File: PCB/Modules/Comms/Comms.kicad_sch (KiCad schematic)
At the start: 51 parts, among them J1 In, J10 1PPS In, J11 32MHz Out, J12 Shield, J13 Shield, J14 BATT +, J15 BATT -, J2 Test, J3 Bus, J4 Bus, J5 SWD, J6 Shield, J7 Shield, J8 Shield, J9 Shield, Q1 Q_PMOS_GSD, U1 STM32WB09KEVx, U2 THVD1420D, U3 MLPF-NRG-01D3, Y1 32MHz, Y2 32.768k

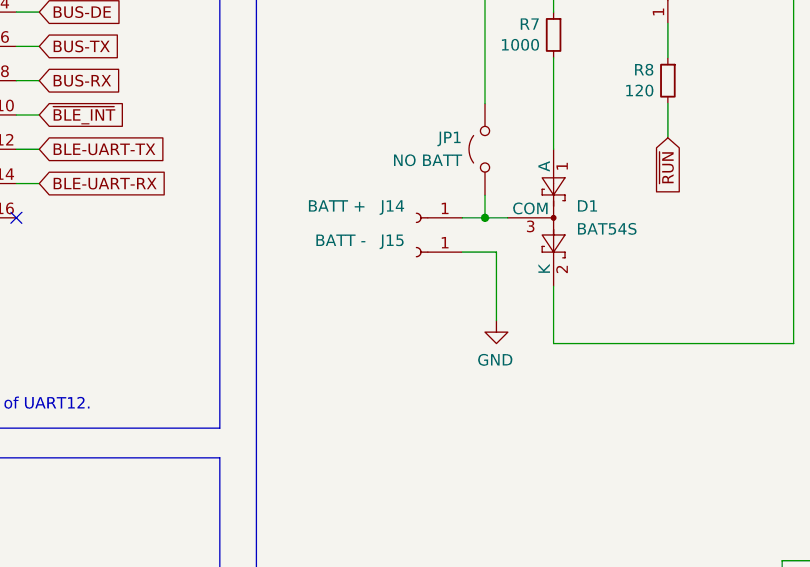
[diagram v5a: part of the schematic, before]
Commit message: feat: Replace bare pads for battery with a cell, incase we want to use a cell holder.
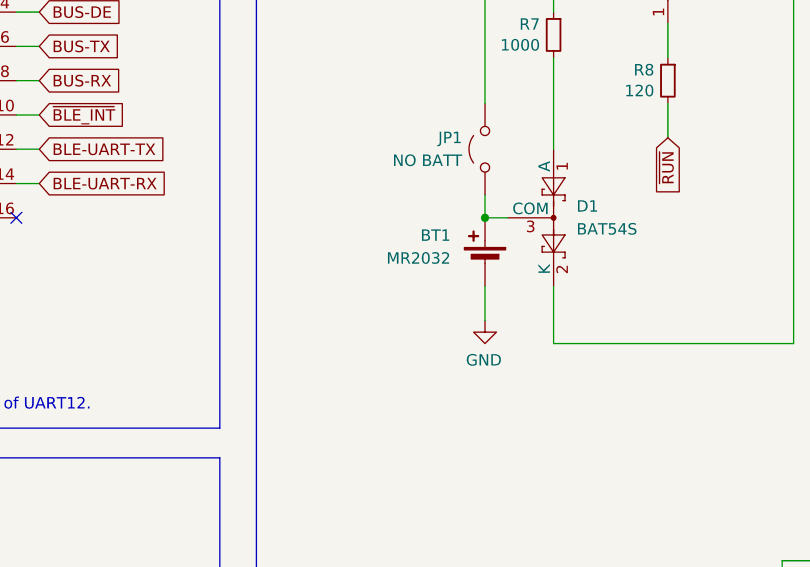
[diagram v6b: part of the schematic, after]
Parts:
- removed J14: BATT +, KTANE:Pad4x2, symbol Connector:Conn_01x01_Socket
- removed J15: BATT -, KTANE:Pad4x2, symbol Connector:Conn_01x01_Socket
- added BT1: MR2032, KTANE:CellHolder, symbol Device:Battery_Cell
- D1: DIGIKEY (none) -> BAT54SLT1GOSCT-ND
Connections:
- net GND: now also BT1.2 (-)
- net at D1.3 (COM), JP1.2 (B): now also BT1.1 (+)
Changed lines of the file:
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@@
 	)
 	(junction
-		(at 111.76 63.5)
-		(diameter 0)
-		(color 0 0 0 0)
-	)
-	(junction
 		(at 80.01 151.13)
 		(diameter 0)
@@
 	)
 	(junction
+		(at 111.76 63.5)
+		(diameter 0)
+		(color 0 0 0 0)
+	)
+	(junction
 		(at 64.77 142.24)
 		(diameter 0)
@@
 	(wire
 		(pts
-			(xy 111.76 60.96) (xy 111.76 63.5)
-		)
-		(stroke
-			(width 0)
-			(type default)
-		)
-	)
-	(wire
-		(pts
 			(xy 102.87 158.75) (xy 100.33 158.75)
 		)
@@
 	(wire
 		(pts
-			(xy 109.22 67.31) (xy 113.03 67.31)
-		)
-		(stroke
-			(width 0)
-			(type default)
-		)
-	)
-	(wire
-		(pts
 			(xy 85.09 156.21) (xy 85.09 163.83)
 		)
@@
 	(wire
 		(pts
-			(xy 113.03 67.31) (xy 113.03 74.93)
+			(xy 111.76 71.12) (xy 111.76 74.93)
 		)
 		(stroke
@@
 	(wire
 		(pts
+			(xy 111.76 60.96) (xy 111.76 63.5)
+		)
+		(stroke
+			(width 0)
+			(type default)
+		)
+	)
+	(wire
+		(pts
 			(xy 157.48 31.75) (xy 157.48 34.29)
 		)
@@
 	(wire
 		(pts
-			(xy 109.22 63.5) (xy 111.76 63.5)
-		)
-		(stroke
-			(width 0)
-			(type default)
-		)
-	)
-	(wire
-		(pts
 			(xy 90.17 151.13) (xy 90.17 148.59)
 		)
@@
 	)
 	(symbol
-		(lib_id "Connector:Conn_01x01_Socket")
-		(at 104.14 63.5 0)
+		(lib_id "Device:Battery_Cell")
+		(at 111.76 68.58 0)
 		(mirror y)
 		(unit 1)
@@
 		(in_pos_files yes)
 		(dnp no)
-		(property "Reference" "J14"
-			(at 102.87 62.2299 0)
+		(property "Reference" "BT1"
+			(at 107.95 65.4684 0)
 			(show_name no)
 			(do_not_autoplace no)
@@
 			)
 		)
-		(property "Value" "BATT +"
-			(at 98.552 62.23 0)
+		(property "Value" "MR2032"
+			(at 107.95 68.0084 0)
 			(show_name no)
 			(do_not_autoplace no)
@@
 			)
 		)
-		(property "Footprint" "KTANE:Pad4x2"
-			(at 104.14 63.5 0)
+		(property "Footprint" "KTANE:CellHolder"
+			(at 111.76 67.056 90)
 			(hide yes)
 			(show_name no)
@@
 		)
 		(property "Datasheet" ""
-			(at 104.14 63.5 0)
+			(at 111.76 67.056 90)
 			(hide yes)
 			(show_name no)
@@
 			)
 		)
-		(property "Description" "Generic connector, single row, 01x01, script generated"
-			(at 104.14 63.5 0)
+		(property "Description" "Single-cell battery"
+			(at 111.76 68.58 0)
 			(hide yes)
 			(show_name no)
@@
 			)
 		)
+		(property "Sim.Device" "V"
+			(at 111.76 68.58 0)
+			(hide yes)
+			(show_name no)
+			(do_not_autoplace no)
+			(effects
+				(font
+					(size 1.27 1.27)
+				)
+			)
+		)
+		(property "Sim.Type" "DC"
+			(at 111.76 68.58 0)
+			(hide yes)
+			(show_name no)
+			(do_not_autoplace no)
+			(effects
+				(font
+					(size 1.27 1.27)
+				)
+			)
+		)
+		(property "Sim.Pins" "1=+ 2=-"
+			(at 111.76 68.58 0)
+			(hide yes)
+			(show_name no)
+			(do_not_autoplace no)
+			(effects
+				(font
+					(size 1.27 1.27)
+				)
+			)
+		)
+		(pin "2"
+		)
 		(pin "1"
 		)
@@
 			(project "Comms"
 				(path "/e63e39d7-6ac0-4ffd-8aa3-1841a4541b55"
-					(reference "J14")
+					(reference "BT1")
 					(unit 1)
 				)
@@
 	)
 	(symbol
-		(lib_id "Connector:Conn_01x01_Socket")
-		(at 104.14 67.31 0)
-		(mirror y)
-		(unit 1)
-		(body_style 1)
-		(exclude_from_sim no)
-		(in_bom yes)
-		(on_board yes)
-		(in_pos_files yes)
-		(dnp no)
-		(property "Reference" "J15"
-			(at 102.87 66.0399 0)
-			(show_name no)
-			(do_not_autoplace no)
-			(effects
-				(font
-					(size 1.27 1.27)
-				)
-				(justify left)
-			)
-		)
-		(property "Value" "BATT -"
-			(at 98.552 66.04 0)
-			(show_name no)
-			(do_not_autoplace no)
-			(effects
-				(font
-					(size 1.27 1.27)
-				)
-				(justify left)
-			)
-		)
-		(property "Footprint" "KTANE:Pad4x2"
-			(at 104.14 67.31 0)
-			(hide yes)
-			(show_name no)
-			(do_not_autoplace no)
-			(effects
-				(font
-					(size 1.27 1.27)
-				)
-			)
-		)
-		(property "Datasheet" ""
-			(at 104.14 67.31 0)
-			(hide yes)
-			(show_name no)
-			(do_not_autoplace no)
-			(effects
-				(font
-					(size 1.27 1.27)
-				)
-			)
-		)
-		(property "Description" "Generic connector, single row, 01x01, script generated"
-			(at 104.14 67.31 0)
-			(hide yes)
-			(show_name no)
-			(do_not_autoplace no)
-			(effects
-				(font
-					(size 1.27 1.27)
-				)
-			)
-		)
-		(pin "1"
-		)
-		(instances
-			(project "Comms"
-				(path "/e63e39d7-6ac0-4ffd-8aa3-1841a4541b55"
-					(reference "J15")
-					(unit 1)
-				)
-			)
-		)
-	)
-	(symbol
 		(lib_id "power:+3.3VP")
 		(at 146.05 29.21 0)
@@
 	(symbol
 		(lib_id "power:GND")
-		(at 113.03 74.93 0)
+		(at 111.76 74.93 0)
 		(mirror y)
 		(unit 1)
@@
 		(dnp no)
 		(property "Reference" "#PWR051"
-			(at 113.03 81.28 0)
+			(at 111.76 81.28 0)
 			(hide yes)
 			(show_name no)
@@
 		)
 		(property "Value" "GND"
-			(at 112.903 79.3242 0)
+			(at 111.633 79.3242 0)
 			(show_name no)
 			(do_not_autoplace no)
@@
 		)
 		(property "Footprint" ""
-			(at 113.03 74.93 0)
+			(at 111.76 74.93 0)
 			(hide yes)
 			(show_name no)
@@
 		)
 		(property "Datasheet" ""
-			(at 113.03 74.93 0)
+			(at 111.76 74.93 0)
 			(hide yes)
 			(show_name no)
@@
 		)
 		(property "Description" "Power symbol creates a global label with name \"GND\" , ground"
-			(at 113.03 74.93 0)
+			(at 111.76 74.93 0)
 			(hide yes)
 			(show_name no)
@@
 			(hide yes)
 			(show_name no)
+			(do_not_autoplace no)
+			(effects
+				(font
+					(size 1.27 1.27)
+				)
+			)
+		)
+		(property "DIGIKEY" "BAT54SLT1GOSCT-ND"
+			(at 119.38 63.5 90)
+			(hide yes)
+			(show_name no)
